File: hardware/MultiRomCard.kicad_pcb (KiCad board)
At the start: 2 copper layers, 131.3 x 100 mm, 29 parts, among them P1 VC4000_Cartridge_Bus, P2 MicroSD_Breakout, P3 DISPLAY, SW1 UP, SW2 DOWN, SW3 SELECT, U1 Arduino_Nano, U10 74HC32, U2 74HC595, U3 74HC595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

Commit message: [PCB] Some last optimizations for v. 0.2.
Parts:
- C1, C2, C3, C4, C5, C6, C7, C8, C9: footprint Capacitors_ThroughHole:C_Disc_D6_P5 -> Capacitors_ThroughHole:C_Rect_L7_W2_P5
- moved C2 2.36 mm to (117.3, 85.4)
- moved P2 2.29 mm to (89.6, 100.6)
- moved C3 1.42 mm to (120.0, 144.0)
- moved C7 1.37 mm to (177.9, 144.2)
- moved C8 1.27 mm to (177.7, 71.5)
- moved C1 1.27 mm to (120.0, 115.9)
- moved C6 1.25 mm to (177.9, 111.0)
- moved C4 1.17 mm to (159.4, 94.7)
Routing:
- net VCC: track 597.8 -> 584.0 mm
- net Net-(R2-Pad1): track 53.2 -> 55.5 mm, vias 1 -> 2
- net Net-(P2-Pad2): track 10.6 -> 12.9 mm
- net Net-(P2-Pad4): track 24.4 -> 26.7 mm
- net Net-(P2-Pad1): track 32.7 -> 35.0 mm
- net Net-(P2-Pad3): track 23.8 -> 26.1 mm
- net GND: track 281.0 -> 283.3 mm
- net /A10: track 99.3 -> 101.2 mm
- net Net-(R3-Pad1): track 58.7 -> 60.0 mm, vias 1 -> 2
- net /A0: track 89.7 -> 88.7 mm
- net Net-(R4-Pad1): track 26.4 -> 25.6 mm

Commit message: [HW] Update PCB to v. 0.3 (include 7-segm display).
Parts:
- added C10: .1uF, Capacitors_ThroughHole:C_Rect_L7_W2_P5, F.Cu at (96.4, 109.0)
- added C11: .1uF, Capacitors_ThroughHole:C_Rect_L7_W2_P5, F.Cu at (85.9, 80.9)
- added P4: JUMPER1, Pin_Headers:Pin_Header_Straight_1x02, F.Cu at (97.6, 141.2)
- added P5: JUMPER2, Pin_Headers:Pin_Header_Straight_1x02, F.Cu at (97.7, 133.8)
- added P6: JUMPER3, Pin_Headers:Pin_Header_Straight_1x02, F.Cu at (97.7, 126.3)
- added P7: JUMPER4, Pin_Headers:Pin_Header_Straight_1x02, F.Cu at (97.6, 118.8)
- added R10: 330, Resistors_ThroughHole:Resistor_Horizontal_RM10mm, F.Cu at (108.7, 64.2)
- added R11: 330, Resistors_ThroughHole:Resistor_Horizontal_RM10mm, F.Cu at (108.7, 61.7)
- added R12: 330, Resistors_ThroughHole:Resistor_Horizontal_RM10mm, F.Cu at (108.7, 59.2)
- added R13: 330, Resistors_ThroughHole:Resistor_Horizontal_RM10mm, F.Cu at (78.5, 58.2)
- added R14: 330, Resistors_ThroughHole:Resistor_Horizontal_RM10mm, F.Cu at (78.5, 55.6)
- added R15: 330, Resistors_ThroughHole:Resistor_Horizontal_RM10mm, F.Cu at (78.5, 53.1)
- added R16: 330, Resistors_ThroughHole:Resistor_Horizontal_RM10mm, F.Cu at (108.7, 54.1)
- added R17: 330, Resistors_ThroughHole:Resistor_Horizontal_RM10mm, F.Cu at (108.7, 51.5)
- added R18: 330, Resistors_ThroughHole:Resistor_Horizontal_RM10mm, F.Cu at (78.5, 60.7)
- added R19: 330, Resistors_ThroughHole:Resistor_Horizontal_RM10mm, F.Cu at (78.5, 63.2)
- added R20: 330, Resistors_ThroughHole:Resistor_Horizontal_RM10mm, F.Cu at (78.5, 50.5)
- added R5: 330, Resistors_ThroughHole:Resistor_Horizontal_RM10mm, F.Cu at (78.5, 65.8)
- added R6: 330, Resistors_ThroughHole:Resistor_Horizontal_RM10mm, F.Cu at (78.5, 68.3)
- added R7: 330, Resistors_ThroughHole:Resistor_Horizontal_RM10mm, F.Cu at (108.7, 56.6)
- added R8: 330, Resistors_ThroughHole:Resistor_Horizontal_RM10mm, F.Cu at (108.7, 69.3)
- added R9: 330, Resistors_ThroughHole:Resistor_Horizontal_RM10mm, F.Cu at (108.7, 66.8)
- added S1: 7SEGM_KB_SC39-11, VC4000_MultiRom:7_Segment_Display_KB_13_10mm, F.Cu at (87.6, 73.7)
- added S2: 7SEGM_KB_SC39-11, VC4000_MultiRom:7_Segment_Display_KB_13_10mm, F.Cu at (87.6, 62.2)
- added U11: 74HC595, Housings_DIP:DIP-16_W7.62mm_LongPads, F.Cu at (104.0, 105.1)
- added U12: 74HC595, Housings_DIP:DIP-16_W7.62mm_LongPads, F.Cu at (77.3, 84.8)
- moved R3 77.9 mm to (126.7, 56.4)
- moved R4 53.4 mm to (124.3, 64.0), turned to 90 degrees
- moved R2 48.3 mm to (126.7, 72.1)
- moved P3 42.8 mm to (104.3, 121.3), turned to 0 degrees
- moved P2 33.7 mm to (123.2, 98.2)
- moved SW1 27.6 mm to (118.8, 75.4)
- moved SW3 27.5 mm to (118.8, 65.3)
- moved SW2 27.3 mm to (118.8, 55.1)
- moved C2 20.0 mm to (137.3, 85.4)
- moved U2 20.0 mm to (147.6, 112.1)
- moved U3 20.0 mm to (147.7, 81.6)
- moved U4 20.0 mm to (147.6, 140.2)
- moved C1 20.0 mm to (140.0, 115.9)
- moved C3 20.0 mm to (140.0, 144.0)
- moved C4 20.0 mm to (179.4, 94.7)
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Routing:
- net VCC: track 584.0 -> 679.4 mm, vias 30 -> 36
- net Net-(R6-Pad2): track 0.00 -> 80.0 mm, vias 0 -> 4
- net Net-(R5-Pad2): track 0.00 -> 69.6 mm, vias 0 -> 4
- net Net-(R17-Pad2): track 0.00 -> 68.5 mm, vias 0 -> 2
- net Net-(P5-Pad1): track 0.00 -> 65.3 mm, vias 0 -> 4
- net Net-(R16-Pad2): track 0.00 -> 65.1 mm, vias 0 -> 2
- net Net-(R20-Pad2): track 0.00 -> 54.8 mm
- net Net-(P6-Pad1): track 0.00 -> 51.0 mm
- net Net-(R7-Pad2): track 0.00 -> 50.3 mm, vias 0 -> 2
- net Net-(P7-Pad1): track 0.00 -> 48.7 mm, vias 0 -> 4
- net Net-(P4-Pad1): track 0.00 -> 47.9 mm
- net GND: track 283.3 -> 330.7 mm
- net Net-(R3-Pad1): track 60.0 -> 15.9 mm, vias 2 -> 0
- net Net-(R15-Pad2): track 0.00 -> 41.6 mm
- net Net-(R13-Pad2): track 0.00 -> 40.5 mm, vias 0 -> 2
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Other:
- board size 131.3 x 100 mm -> 160 x 100 mm
- board text added: "VC4000 MultiROM v0.3"
- board text removed: "VC4000 MultiROM v0.2"

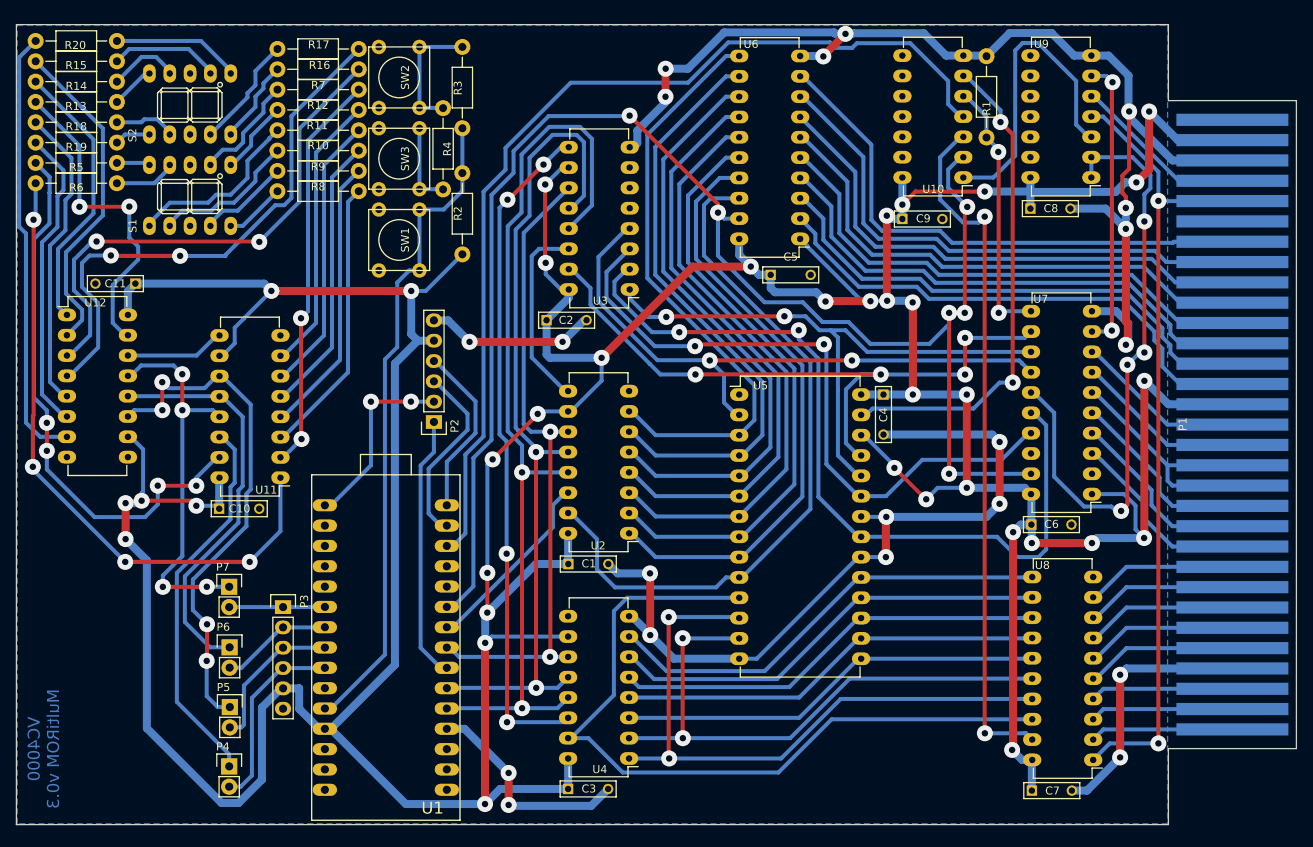
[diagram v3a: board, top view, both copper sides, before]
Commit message: [PCB] New cap footprint with larger pads...
- ... should allow for easier hand soldering.
- Some minor reroutings to decrease copper loss when etching the board.
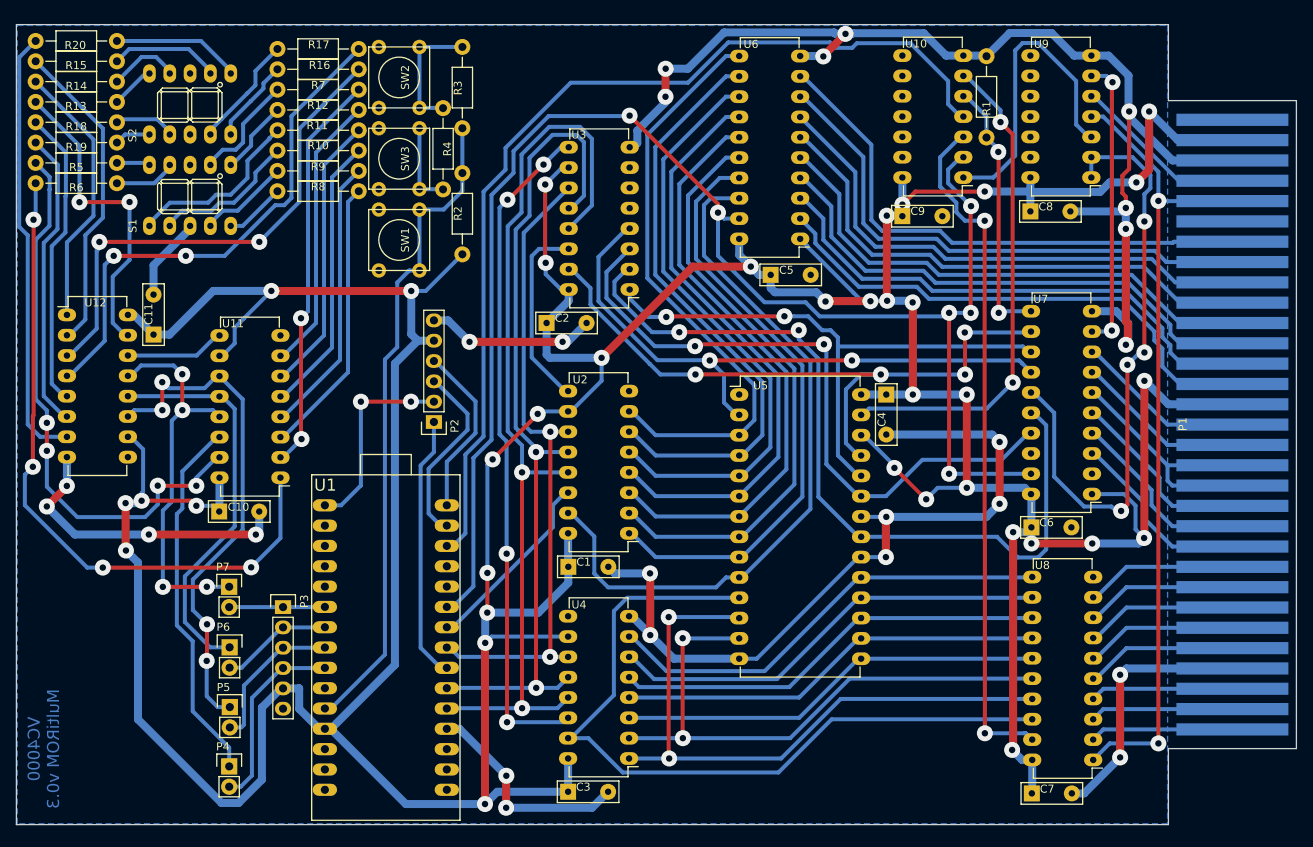
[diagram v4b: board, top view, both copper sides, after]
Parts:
- C1, C10, C11, C2, C3, C4, C5, C6, C7, C8, C9: footprint Capacitors_ThroughHole:C_Rect_L7_W2_P5 -> VC4000_MultiRom:C_Rect_L7_W2_P5_DIY
- moved C11 6.77 mm to (88.1, 87.2), turned to 90 degrees
- moved C3 0.35 mm to (140.0, 144.4)
- moved C4 0.35 mm to (179.7, 94.7)
- moved C9 0.35 mm to (181.7, 72.4)
- moved C1 0.35 mm to (140.0, 116.3)
- moved C10 0.35 mm to (96.4, 109.4)
- moved C2 0.35 mm to (137.3, 85.8)
- moved C6 0.35 mm to (197.9, 111.3)
- moved C7 0.35 mm to (197.9, 144.6)
- moved C8 0.35 mm to (197.7, 71.9)
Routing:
- net GND: track 330.7 -> 377.8 mm, vias 20 -> 24
- net Net-(R6-Pad2): track 80.0 -> 85.1 mm
- net Net-(R17-Pad2): track 68.5 -> 64.9 mm
- net OEVCBUS: track 192.8 -> 190.0 mm
- net Net-(R16-Pad2): track 65.1 -> 62.8 mm
- net VCC: track 679.4 -> 681.3 mm
- net Net-(R15-Pad2): track 41.6 -> 39.8 mm
- net /A9: track 74.1 -> 72.4 mm
- net Net-(P4-Pad1): track 47.9 -> 46.3 mm
- net Net-(P2-Pad2): track 23.7 -> 25.2 mm
- net CEDBUS: track 87.2 -> 86.0 mm
- net Net-(R5-Pad2): track 69.6 -> 70.7 mm
- net Net-(P5-Pad1): track 65.3 -> 64.2 mm
- net Net-(R14-Pad2): track 34.5 -> 33.5 mm
- net Net-(R13-Pad2): track 40.5 -> 39.6 mm
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
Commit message: added ground plane on front side
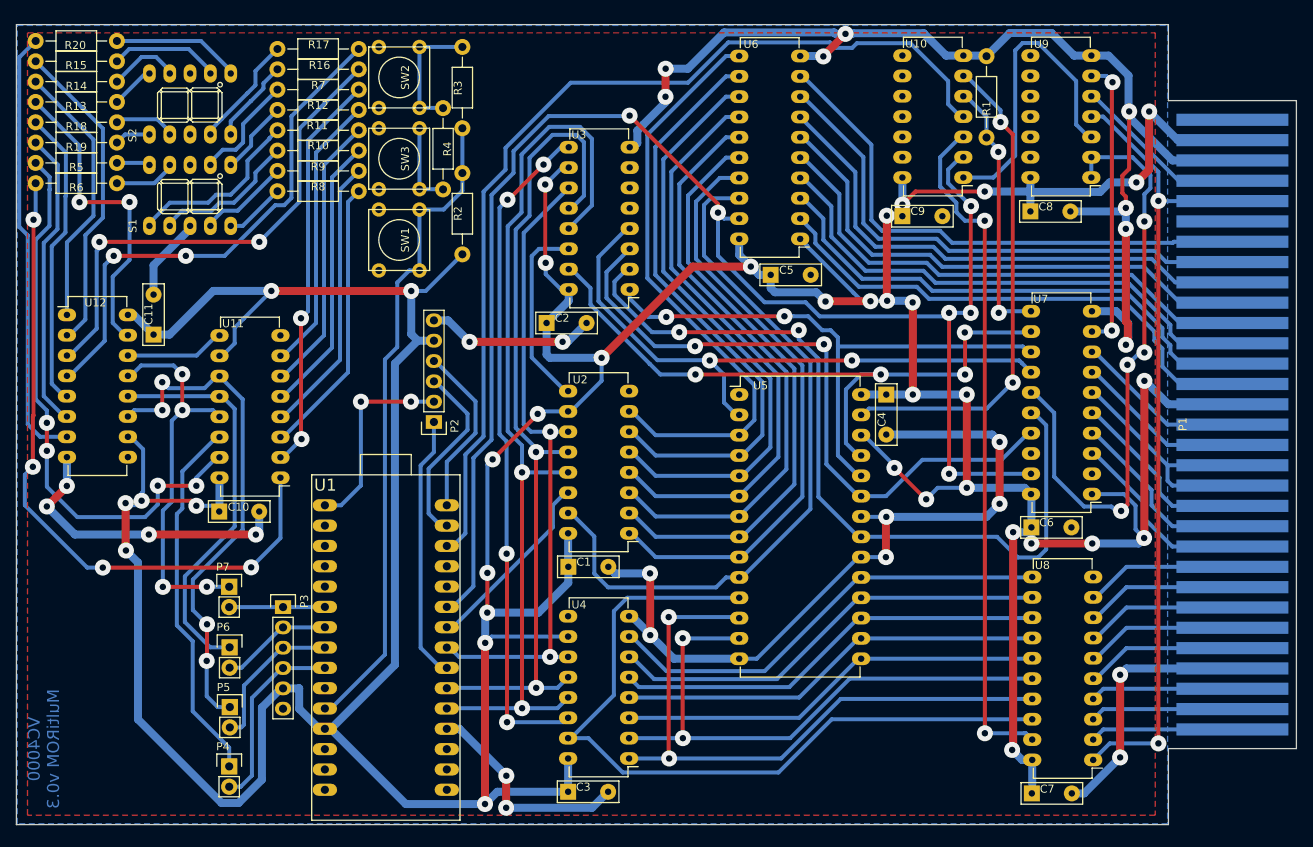
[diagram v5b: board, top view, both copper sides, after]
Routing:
- added copper zone on F.Cu, net GND
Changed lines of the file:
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@@
-(kicad_pcb (version 4) (host pcbnew "(2015-08-28 BZR 6132)-product")
+(kicad_pcb (version 4) (host pcbnew "(2015-08-13 BZR 6091)-product")
   (general
     (links 228)
@@
   (layers
     (0 F.Cu signal)
-    (31 B.Cu signal)
+    (31 B.Cu signal hide)
     (32 B.Adhes user)
     (33 F.Adhes user)
@@
       )
     )
+  )
+  (zone (net 20) (net_name GND) (layer F.Cu) (hatch edge 0.508)
+    (connect_pads (clearance 0.508))
+    (min_thickness 0.254)
+    (fill yes (arc_segments 16) (thermal_gap 0.508) (thermal_bridge_width 0.508))
+    (polygon
+      (pts
+        (xy 72.39 49.53) (xy 213.36 49.53) (xy 213.36 147.32) (xy 72.39 147.32)
+      )
+    )

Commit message: [PCB] Changes for v0.4
- Arduino USB port to the border of the mainboard
- Controls to the top
- Add PDF printout of front copper layer
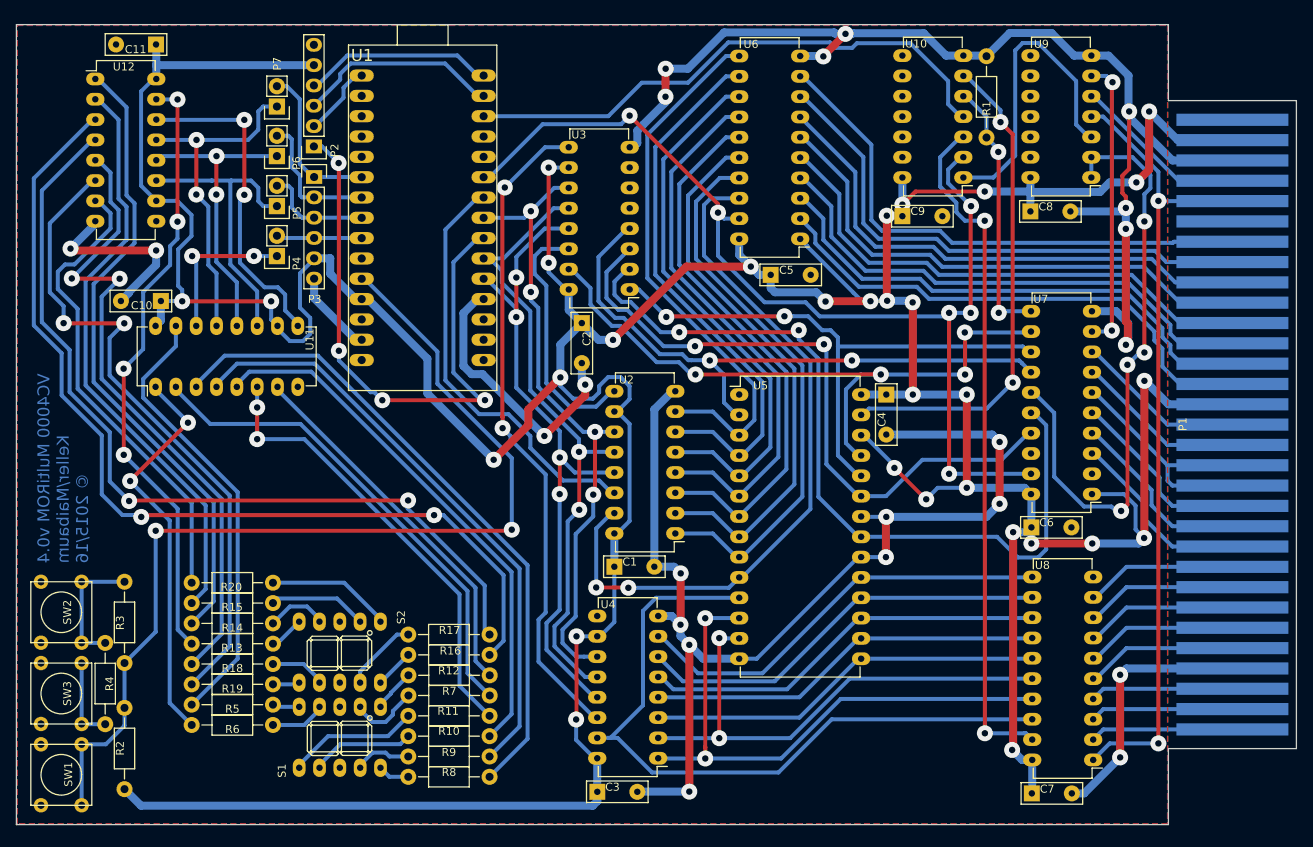
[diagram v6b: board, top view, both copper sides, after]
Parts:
- moved R3 79.1 mm to (84.5, 123.2)
- moved R4 79.1 mm to (82.1, 130.9)
- moved R2 79.1 mm to (84.5, 139.0)
- moved SW1 79.1 mm to (76.6, 142.3)
- moved SW2 79.1 mm to (76.6, 122.0)
- moved SW3 79.1 mm to (76.6, 132.1)
- moved R7 77.5 mm to (125.1, 132.4)
- moved R10 75.0 mm to (125.1, 137.4)
- moved R16 75.0 mm to (125.1, 127.3)
- moved R17 75.0 mm to (125.1, 124.7)
- moved R8 75.0 mm to (125.1, 142.5)
- moved R9 75.0 mm to (125.1, 140.0)
- moved R11 75.0 mm to (125.1, 134.9)
- moved R12 72.5 mm to (125.1, 129.8)
- moved S2 71.0 mm to (106.3, 130.8)
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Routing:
- net VCC: track 681.3 -> 609.6 mm, vias 36 -> 30
- net Net-(R16-Pad2): track 62.8 -> 119.0 mm
- net OEVCBUS: track 190.0 -> 134.2 mm
- net WESRAM: track 121.9 -> 69.8 mm
- net Net-(R8-Pad2): track 35.0 -> 82.5 mm
- net Net-(R14-Pad2): track 33.5 -> 79.8 mm
- net Net-(R19-Pad2): track 37.5 -> 82.8 mm, vias 0 -> 2
- net Net-(R18-Pad2): track 37.5 -> 81.5 mm, vias 0 -> 2
- net Net-(R17-Pad2): track 64.9 -> 108.8 mm
- net Net-(R2-Pad1): track 82.6 -> 123.8 mm, vias 0 -> 2
- net Net-(R9-Pad2): track 35.0 -> 74.9 mm
- net Net-(P2-Pad1): track 33.2 -> 73.2 mm, vias 0 -> 4
- net Net-(R13-Pad2): track 39.6 -> 77.0 mm, vias 2 -> 4
- net Net-(R6-Pad2): track 85.1 -> 50.1 mm, vias 4 -> 2
- net Net-(R15-Pad2): track 39.8 -> 73.9 mm
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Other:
- board text added: "VC4000 MultiROM v0.4 Keller/Maibaum © 2015/16"
- board text removed: "VC4000 MultiROM v0.3"
